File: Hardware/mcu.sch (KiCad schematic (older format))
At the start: 22 parts, among them J1 SWD_programming, U6 CY8C4246AZI-L445, Y1 Crystal

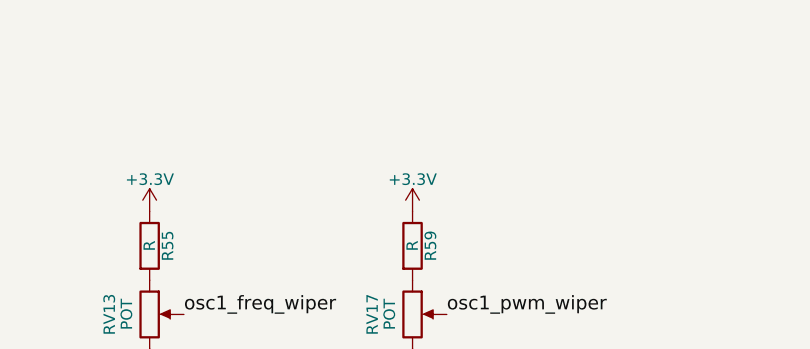
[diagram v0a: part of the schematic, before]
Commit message: add VREF to all single supply op amps
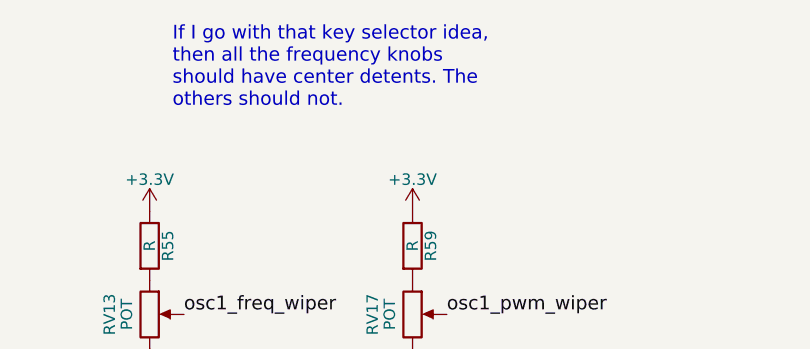
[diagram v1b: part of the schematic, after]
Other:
- note added: "If I go with that key selector idea, \nthen all the frequency knobs \nshould have center detents. The \nothers should not."
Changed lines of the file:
@@
 $Descr A4 11693 8268
 encoding utf-8
-Sheet 8 8
+Sheet 7 7
 Title ""
 Date ""
@@
 Text HLabel 10400 3850 2    60   Output ~ 0
 envelope_pwm_4
+Text Notes 7650 1250 0    60   ~ 0
+If I go with that key selector idea, \nthen all the frequency knobs \nshould have center detents. The \nothers should not.
 $EndSCHEMATC

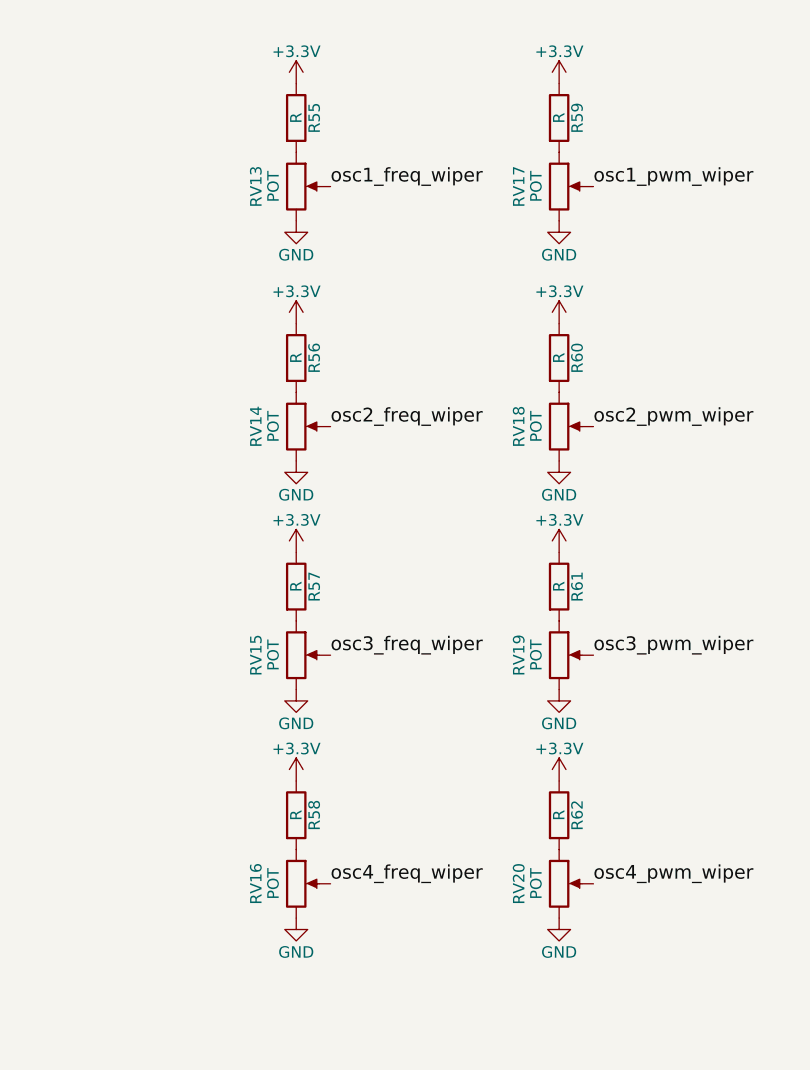
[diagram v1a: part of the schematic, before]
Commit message: begin to add taper to potentiometers. I think they're all right, but some tapers may change under test.
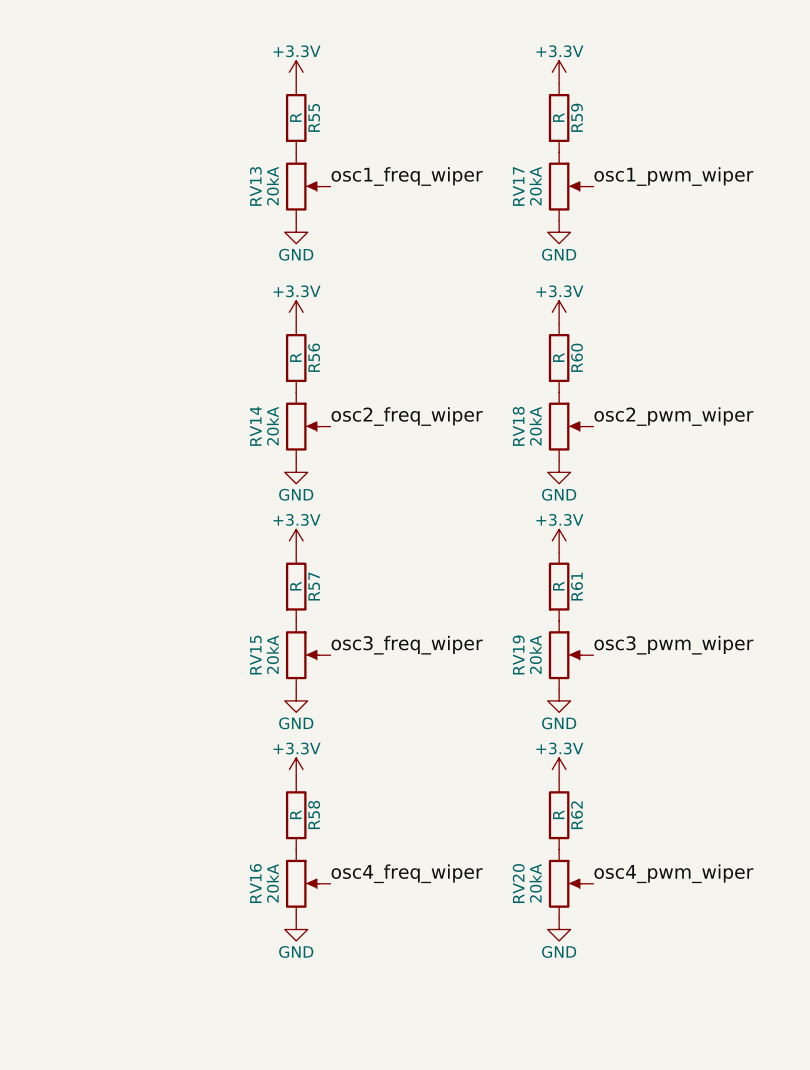
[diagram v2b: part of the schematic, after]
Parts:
- RV13, RV14, RV15, RV16, RV17, RV18, RV19, RV20: value POT -> 20kA
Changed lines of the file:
@@
 P 7550 2150
 F 0 "RV13" V 7375 2150 50  0000 C CNN
-F 1 "POT" V 7450 2150 50  0000 C CNN
+F 1 "20kA" V 7450 2150 50  0000 C CNN
 F 2 "" H 7550 2150 50  0001 C CNN
 F 3 "" H 7550 2150 50  0001 C CNN
@@
 P 8700 2150
 F 0 "RV17" V 8525 2150 50  0000 C CNN
-F 1 "POT" V 8600 2150 50  0000 C CNN
+F 1 "20kA" V 8600 2150 50  0000 C CNN
 F 2 "" H 8700 2150 50  0001 C CNN
 F 3 "" H 8700 2150 50  0001 C CNN
@@
 P 7550 3200
 F 0 "RV14" V 7375 3200 50  0000 C CNN
-F 1 "POT" V 7450 3200 50  0000 C CNN
+F 1 "20kA" V 7450 3200 50  0000 C CNN
 F 2 "" H 7550 3200 50  0001 C CNN
 F 3 "" H 7550 3200 50  0001 C CNN
@@
 P 8700 3200
 F 0 "RV18" V 8525 3200 50  0000 C CNN
-F 1 "POT" V 8600 3200 50  0000 C CNN
+F 1 "20kA" V 8600 3200 50  0000 C CNN
 F 2 "" H 8700 3200 50  0001 C CNN
 F 3 "" H 8700 3200 50  0001 C CNN
@@
 P 7550 4200
 F 0 "RV15" V 7375 4200 50  0000 C CNN
-F 1 "POT" V 7450 4200 50  0000 C CNN
+F 1 "20kA" V 7450 4200 50  0000 C CNN
 F 2 "" H 7550 4200 50  0001 C CNN
 F 3 "" H 7550 4200 50  0001 C CNN
@@
 P 8700 4200
 F 0 "RV19" V 8525 4200 50  0000 C CNN
-F 1 "POT" V 8600 4200 50  0000 C CNN
+F 1 "20kA" V 8600 4200 50  0000 C CNN
 F 2 "" H 8700 4200 50  0001 C CNN
 F 3 "" H 8700 4200 50  0001 C CNN
@@
 P 7550 5200
 F 0 "RV16" V 7375 5200 50  0000 C CNN
-F 1 "POT" V 7450 5200 50  0000 C CNN
+F 1 "20kA" V 7450 5200 50  0000 C CNN
 F 2 "" H 7550 5200 50  0001 C CNN
 F 3 "" H 7550 5200 50  0001 C CNN
@@
 P 8700 5200
 F 0 "RV20" V 8525 5200 50  0000 C CNN
-F 1 "POT" V 8600 5200 50  0000 C CNN
+F 1 "20kA" V 8600 5200 50  0000 C CNN
 F 2 "" H 8700 5200 50  0001 C CNN
 F 3 "" H 8700 5200 50  0001 C CNN

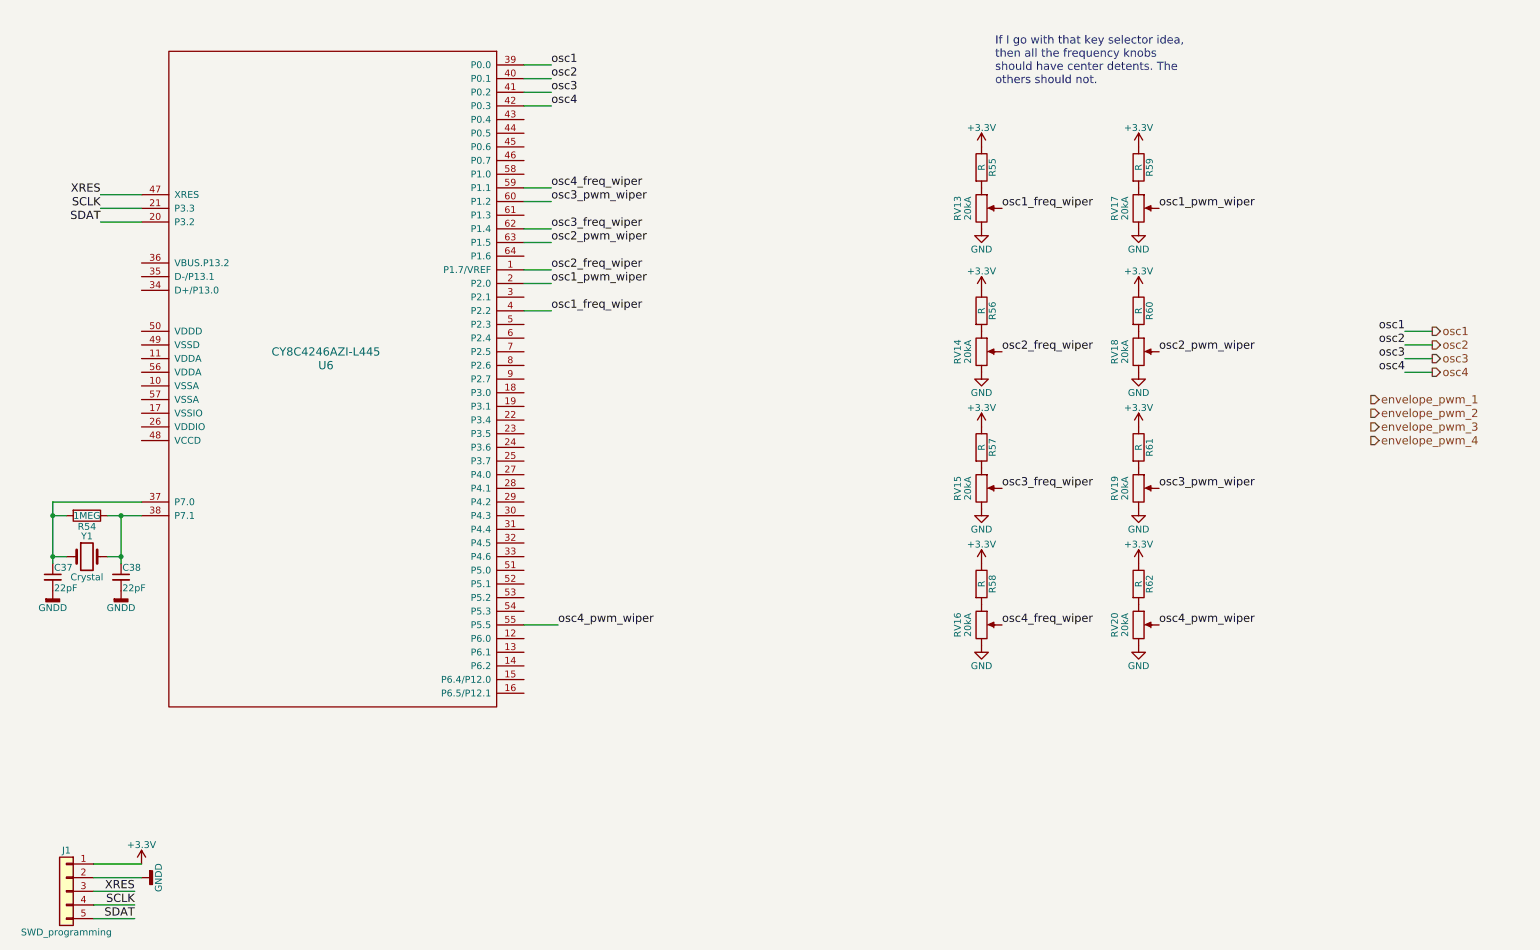
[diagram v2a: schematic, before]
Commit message: add freq and pulse width pots for 8 oscillators. Still needs to be tested on dev board and built, but I wanted to go ahead and add them to the schematic as an option.
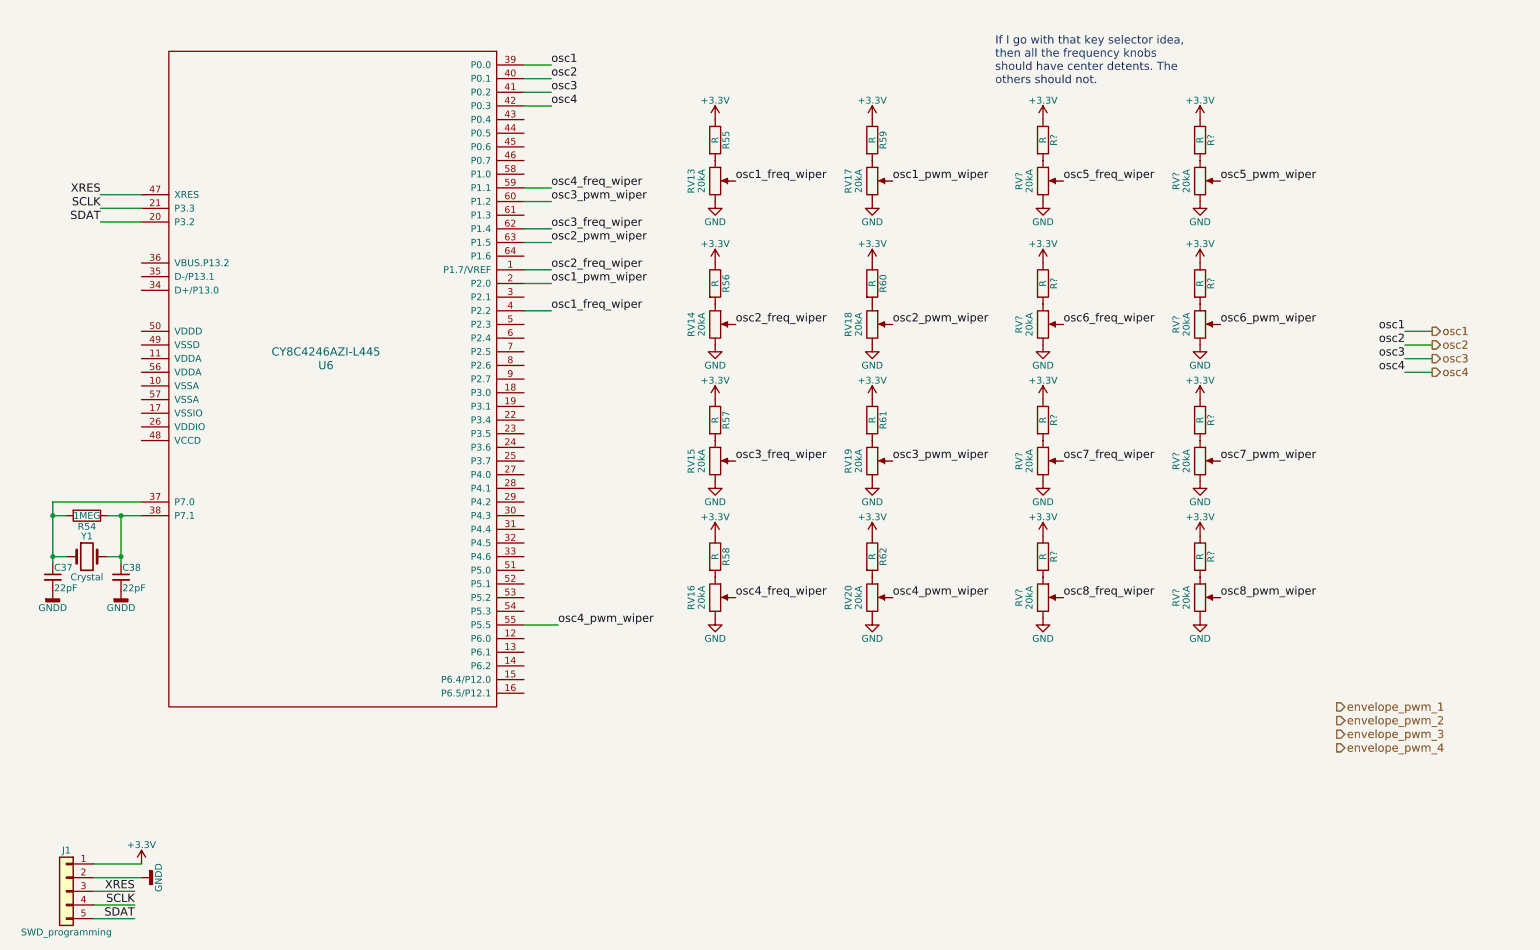
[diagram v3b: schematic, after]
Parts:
- added R? (x8): R, symbol R
- added RV? (x8): 20kA, symbol POT
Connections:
- net +3V3: now also R?.1, R?.1, R?.1, R?.1, R?.1, R?.1, R?.1, R?.1
- net GND: now also RV?.3, RV?.3, RV?.3, RV?.3, RV?.3, RV?.3, RV?.3, RV?.3
- new net: R?.2, RV?.1 (x8)
- new net osc5_freq_wiper: RV?.2
- new net osc5_pwm_wiper: RV?.2
- new net osc6_freq_wiper: RV?.2
- new net osc6_pwm_wiper: RV?.2
- new net osc7_freq_wiper: RV?.2
- new net osc7_pwm_wiper: RV?.2
- new net osc8_freq_wiper: RV?.2
- new net osc8_pwm_wiper: RV?.2
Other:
- moved on the sheet: R55, R56, R57, R58, R59, R60, R61, R62, RV13, RV14, RV15, RV16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

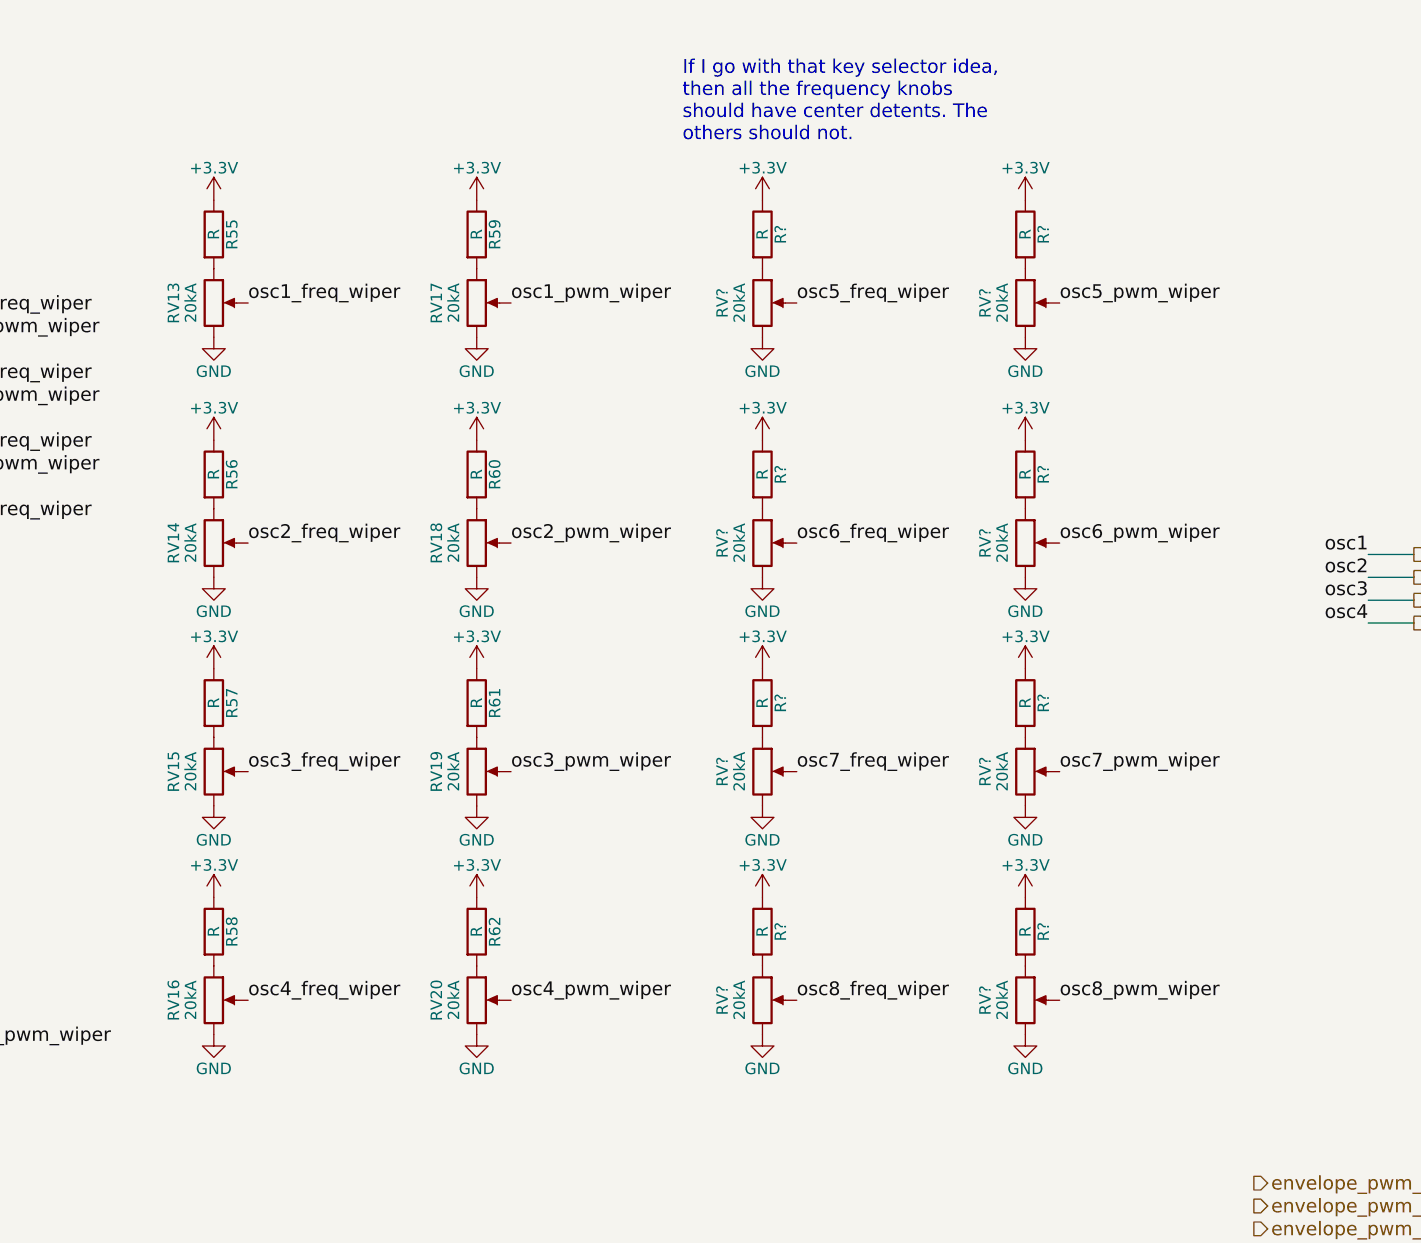
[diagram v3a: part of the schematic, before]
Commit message: change back to 4 oscillators, add speed control. One pot for each oscillator will control both attack and release times simultaneously. This is simpler than a full ADSR for each channel, but still allows more flexibility than a fast/slow switch.
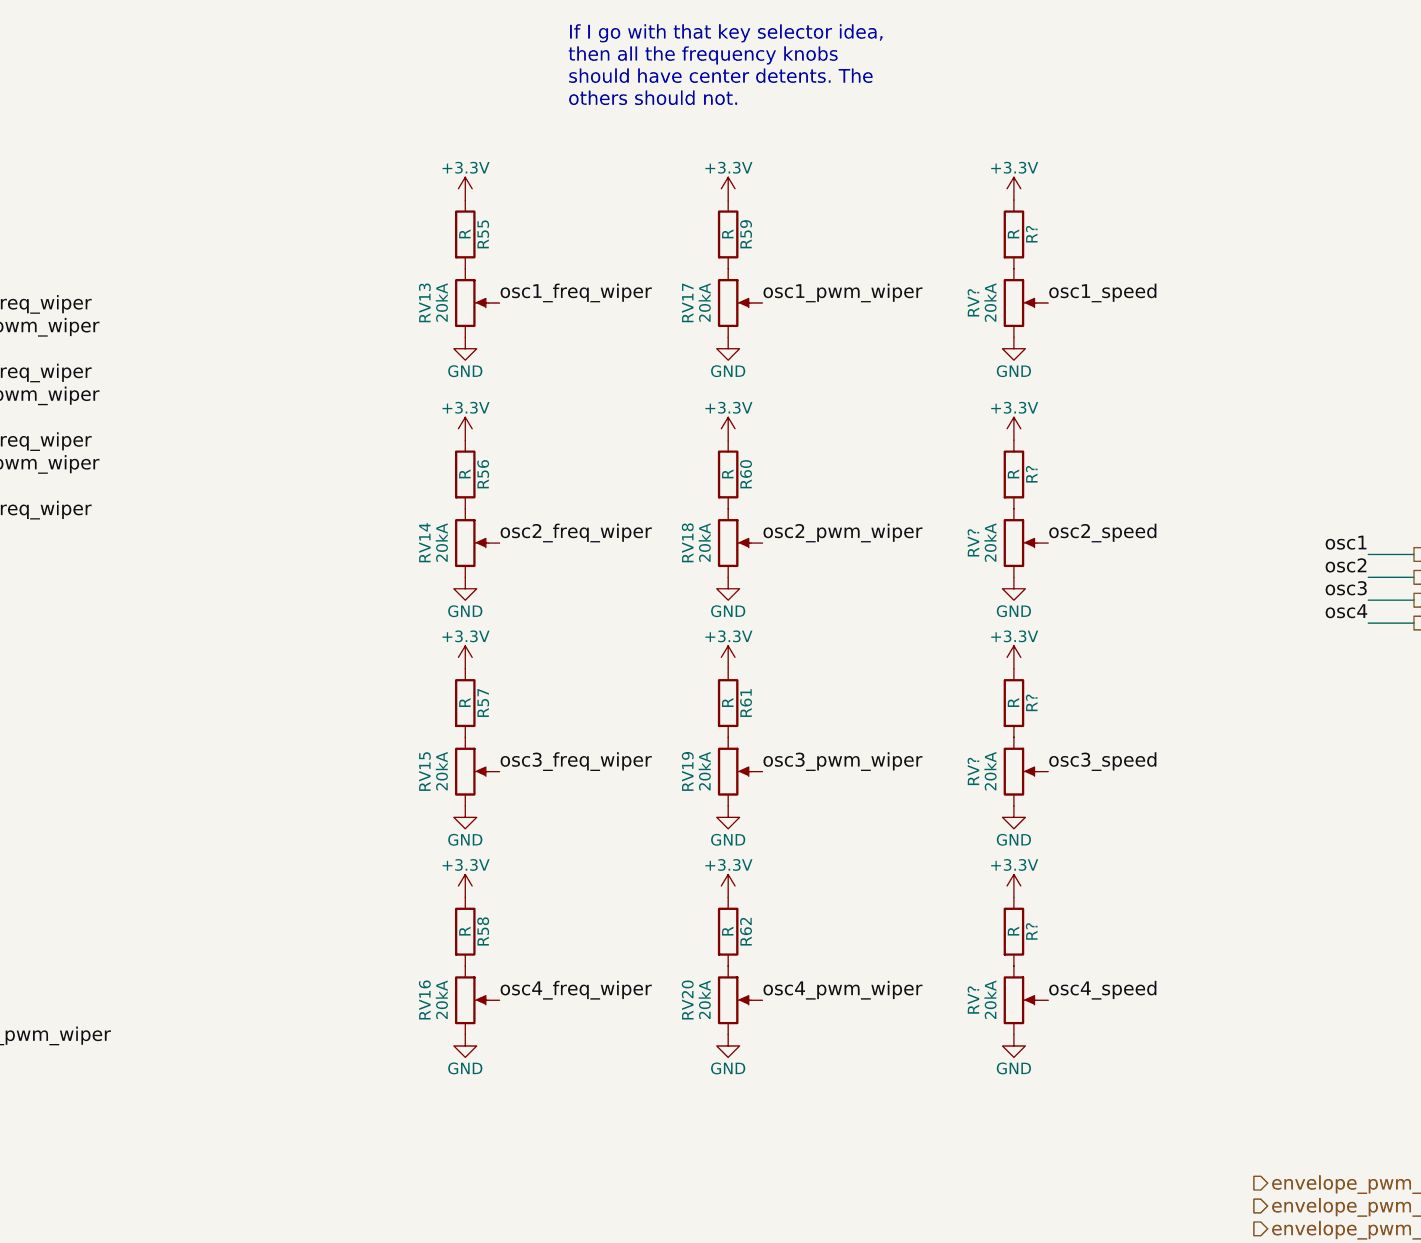
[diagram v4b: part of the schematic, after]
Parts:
- removed R? (x4): R, symbol R
- removed RV? (x4): 20kA, symbol POT
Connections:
- net osc5_freq_wiper renamed osc1_speed
- net osc6_freq_wiper renamed osc2_speed
- net osc7_freq_wiper renamed osc3_speed
- net osc8_freq_wiper renamed osc4_speed
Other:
- moved on the sheet: R55, R56, R57, R58, R59, R60, R61, R62, R?, RV13, RV14, RV15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
